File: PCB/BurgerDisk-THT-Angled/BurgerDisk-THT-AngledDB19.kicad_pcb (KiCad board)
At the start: 2 copper layers, 93.7 x 73.4 mm, 18 parts, among them J1 Daisy port in, J2 MicroSD module, J3 UART, J4 Daisy port out, U1 PC817

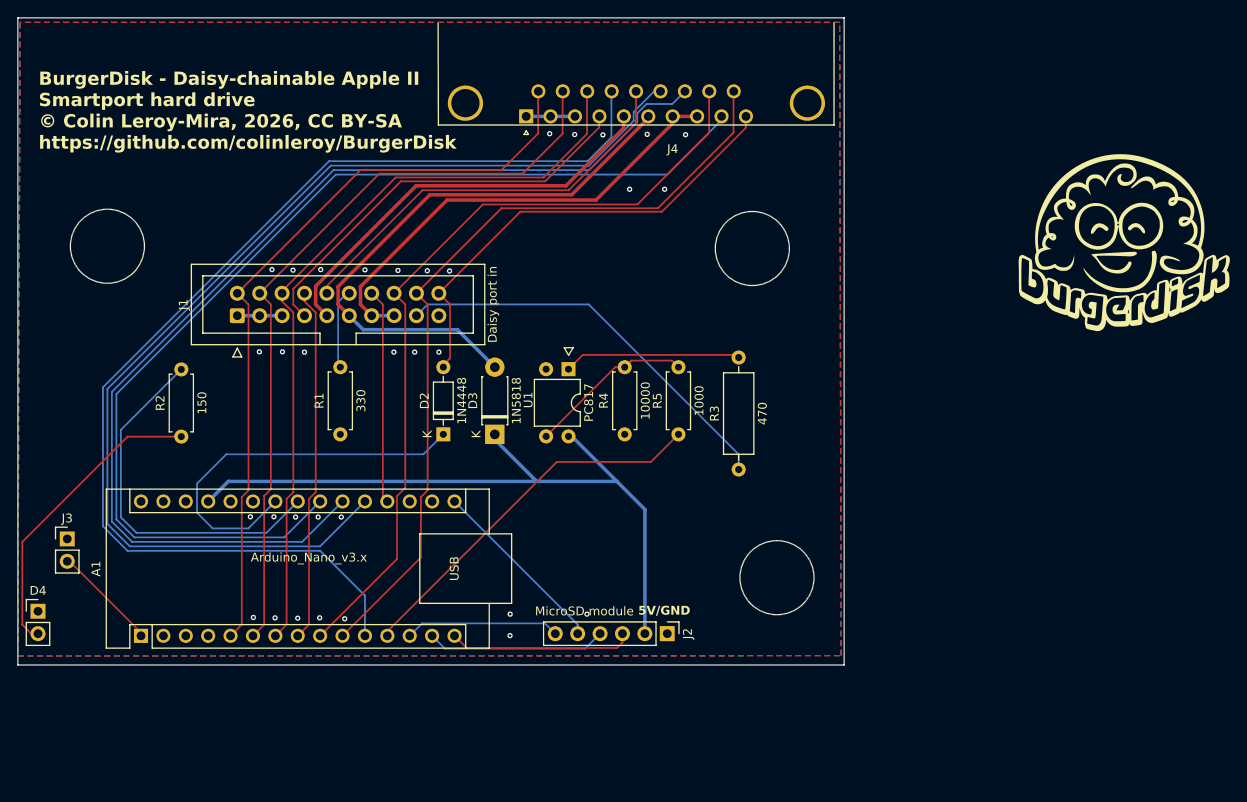
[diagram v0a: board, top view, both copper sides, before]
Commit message: Make PCBs closer to one another
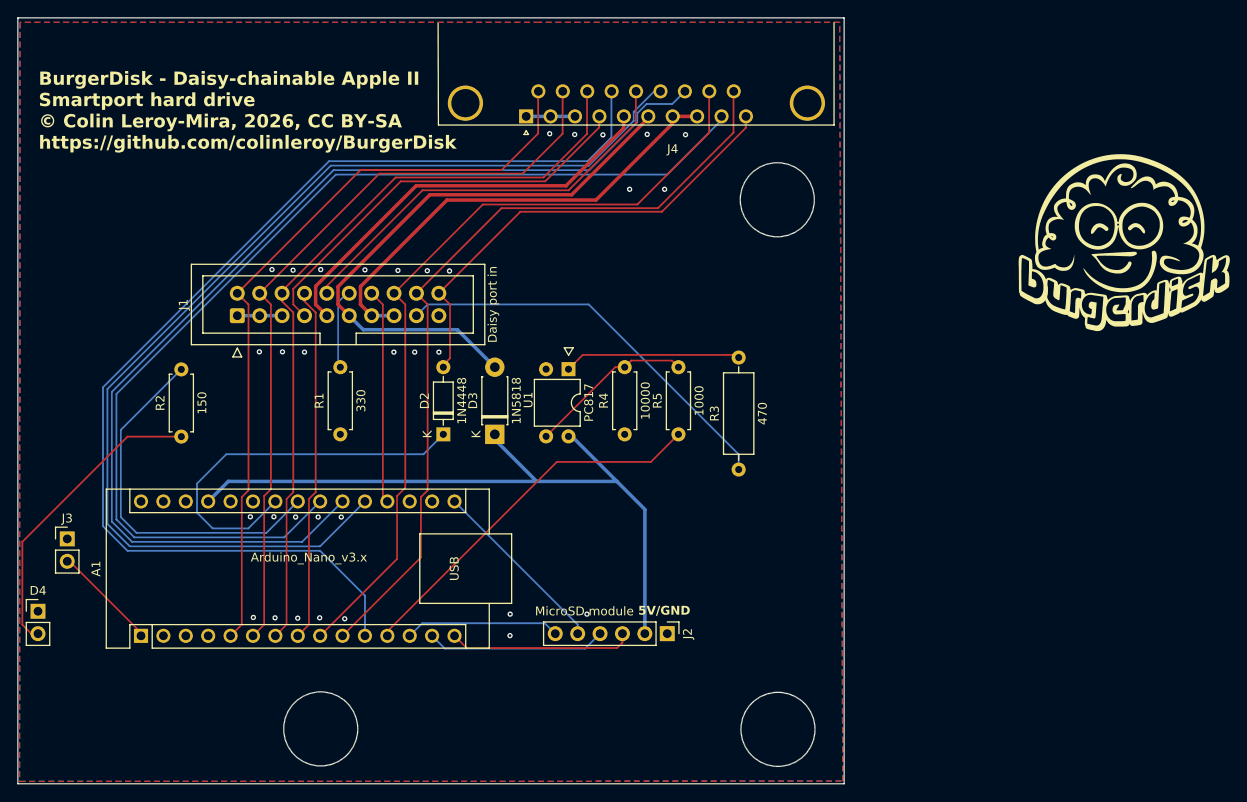
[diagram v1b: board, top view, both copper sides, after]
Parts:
- removed the REF** at (154.2, 64.0)
- removed the REF** at (81.0, 63.8)
- removed the REF** at (157.0, 101.3)
- added REF**: MountingHole_8.4mm_M8, MountingHole:MountingHole_8.4mm_M8, F.Cu at (105.2, 118.5)
- added REF**: MountingHole_8.4mm_M8, MountingHole:MountingHole_8.4mm_M8, F.Cu at (157.0, 58.5)
- added REF**: MountingHole_8.4mm_M8, MountingHole:MountingHole_8.4mm_M8, F.Cu at (157.1, 118.6)
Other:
- board size 93.7 x 73.4 mm -> 93.7 x 86.9 mm
